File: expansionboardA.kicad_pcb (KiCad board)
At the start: 2 copper layers, 111 x 109.4 mm, 40 parts, among them J1 DEBUG, J2 USB_A_Stacked, J3 HDMI_A, P1 USB_C_Plug, U1 MAX3420EECJ, U2 GPIO_U2, U3 AMS1117-3.3, U4 GPIO_U4, U5 MCP3008T-I/SL, U6 TLV320AIC23BIPW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

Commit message: Updatre board version
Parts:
- removed AU2: SJ-3523-SMT-TR, SJ-3523-SMT-TR:CUI_SJ-3523-SMT-TR
- removed D6: LED, LED_SMD:LED_1206_3216Metric_Pad1.42x1.75mm_HandSolder
- added C10: 0.1uf, Capacitor_SMD:C_0603_1608Metric_Pad1.08x0.95mm_HandSolder, B.Cu at (56.7, 76.6)
- added C11: 3.3uf, Capacitor_THT:CP_Radial_D5.0mm_P2.50mm, F.Cu at (57.7, 72.2)
- added C12: 10uf, Capacitor_THT:CP_Radial_D5.0mm_P2.50mm, F.Cu at (65.6, 76.0)
- added C13: 3.3uf, Capacitor_THT:CP_Radial_D5.0mm_P2.50mm, F.Cu at (98.3, 34.2)
- added C14: 3.3uf, Capacitor_THT:CP_Radial_D5.0mm_P2.50mm, F.Cu at (98.3, 24.6)
- added C8: 1uf ceramic, Capacitor_SMD:C_0603_1608Metric_Pad1.08x0.95mm_HandSolder, F.Cu at (110.5, 28.2)
- added C9: 1uf ceramic, Capacitor_SMD:C_0603_1608Metric_Pad1.08x0.95mm_HandSolder, F.Cu at (110.5, 37.6)
- added R11: 10KOhm, Resistor_SMD:R_0603_1608Metric_Pad0.98x0.95mm_HandSolder, F.Cu at (105.9, 37.6)
- added R12: 470Ohm, Resistor_SMD:R_0603_1608Metric_Pad0.98x0.95mm_HandSolder, F.Cu at (105.9, 34.1)
- added R13: 470Ohm, Resistor_SMD:R_0603_1608Metric_Pad0.98x0.95mm_HandSolder, F.Cu at (105.9, 24.6)
- added R14: 10KOhm, Resistor_SMD:R_0603_1608Metric_Pad0.98x0.95mm_HandSolder, F.Cu at (105.9, 28.2)
- added R8: R33_ohm, Resistor_SMD:R_0603_1608Metric_Pad0.98x0.95mm_HandSolder, F.Cu at (110.5, 34.1)
- AU1: moved to B.Cu
- U6: value TLV320AIC23BIPW -> CS4344-CZZR; footprint TLV320AIC23BIPW:SOP65P640X120-28N -> footprints:CIR_3TSSOP-10; moved to B.Cu
- moved R7 58.8 mm to (110.5, 24.6), turned to 0 degrees
- moved D5 19.2 mm to (74.5, 25.8), turned to 180 degrees
- moved D4 16.6 mm to (74.5, 29.2), turned to 180 degrees
- moved D3 15.1 mm to (74.5, 32.6), turned to 180 degrees
- moved D2 15.0 mm to (74.5, 36.0), turned to 180 degrees
- moved AU1 14.8 mm to (129.0, 29.2)
- moved R6 13.9 mm to (68.7, 25.8), turned to 0 degrees
- moved R5 9.96 mm to (68.7, 29.2), turned to 0 degrees
- moved R4 7.14 mm to (68.7, 32.6), turned to 0 degrees
- moved R3 6.99 mm to (68.7, 36.0), turned to 0 degrees
- moved U6 6.54 mm to (59.8, 81.7), turned to 0 degrees
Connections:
- AU1 pad 2: HPOUTRIGHT -> Net-(AU1-Pad2)
- AU1 pad 3: HPOUTLEFT -> Net-(AU1-Pad3)
- R7 pad 1: LED4 -> LEFTOUT
- R7 pad 2: Net-(D6-A) -> Net-(AU1-Pad3)
- U2 pad 29: I2SCLK -> AU_SDIN
- U2 pad 31: I2SDIN -> AU_SCLK
- U2 pad 33: ASCLK -> AU_LRCLK
- U2 pad 35: ASDIN -> AU_MCLK
- U2 pad 37: AMODE -> unconnected-(U2-Pin_37-Pad37)
- U2 pad 39: ACS -> unconnected-(U2-Pin_39-Pad39)
- U2 pad 53: LED4 -> unconnected-(U2-Pin_53-Pad53)
- U6 pad 1: /input3v3 -> AU_SDIN
- U6 pad 10: HPOUTRIGHT -> /AR
- U6 pad 2: unconnected-(U6-CLKOUT-Pad2) -> AU_SCLK
- U6 pad 3: I2SCLK -> AU_LRCLK
- U6 pad 4: I2SDIN -> AU_MCLK
- U6 pad 5: unconnected-(U6-LRCIN-Pad5) -> Net-(U6-VQ)
- U6 pad 6: unconnected-(U6-DOUT-Pad6) -> Net-(U6-FILT+)
- U6 pad 7: unconnected-(U6-LRCOUT-Pad7) -> /AL
- U6 pad 8: /input3v3 -> GND
- U6 pad 9: HPOUTLEFT -> unconnected-(U6-VA-Pad9)
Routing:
- net HPOUTLEFT: track 91.9 -> 0.00 mm, vias 2 -> 0
- net LINEOUTLEFT: track 91.7 -> 0.00 mm, vias 2 -> 0
- net LINEOUTRIGHT: track 91.6 -> 0.00 mm, vias 2 -> 0
- net HPOUTRIGHT: track 91.4 -> 0.00 mm, vias 2 -> 0
- net /AL: track 0.00 -> 83.0 mm, vias 0 -> 1
- net /AR: track 0.00 -> 78.3 mm, vias 0 -> 1
- net LED4: track 29.6 -> 0.00 mm
- net Net-(AU1-Pad3): track 0.00 -> 20.7 mm, vias 0 -> 1
- net I2SCLK: track 18.1 -> 0.00 mm, vias 1 -> 0
- net I2SDIN: track 17.4 -> 0.00 mm, vias 1 -> 0
- net /input3v3: track 191.2 -> 174.6 mm, vias 8 -> 6
- net Net-(AU1-Pad2): track 0.00 -> 13.3 mm, vias 0 -> 1
- net ASCLK: track 11.3 -> 0.00 mm
- net AU_LRCLK: track 0.00 -> 11.0 mm
- net AU_SDIN: track 0.00 -> 11.0 mm
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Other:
- board text added: "GND D+ D- 5V"
- board text removed: "5V D- D+ GND"
- board text removed: "LINE OUT"

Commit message: Updated board files
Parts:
- moved D5 24.3 mm to (50.4, 22.7), turned to -90 degrees
- moved D4 21.7 mm to (53.8, 22.7), turned to -90 degrees
- moved D3 19.9 mm to (57.2, 22.7), turned to -90 degrees
- moved D2 19.3 mm to (60.6, 22.7), turned to -90 degrees
- moved R6 18.5 mm to (50.4, 28.5), turned to 90 degrees
- moved R5 14.9 mm to (53.8, 28.5), turned to 90 degrees
- moved R4 12.2 mm to (57.2, 28.5), turned to 90 degrees
- moved R3 11.0 mm to (60.6, 28.5), turned to 90 degrees
- moved C3 1.80 mm to (89.2, 86.9)
- moved C4 1.80 mm to (81.9, 94.1)
- moved Y1 1.80 mm to (84.6, 91.5)
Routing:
- net LED3: track 41.6 -> 44.7 mm
- net USBD1_N: track 31.9 -> 34.9 mm
- net USBD1_P: track 31.8 -> 34.7 mm
- net Net-(U1-XO): track 10.9 -> 8.90 mm
- net LED2: track 40.2 -> 42.1 mm
- net Net-(U1-XI): track 11.3 -> 9.47 mm
- net LED0: track 41.0 -> 42.3 mm
- net LED1: track 39.8 -> 40.9 mm
- net Net-(U6-VQ): track 10.0 -> 10.7 mm
- net GND: vias 28 -> 27

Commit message: Updated board to fix some issues
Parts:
- added J4: FAN, Connector_PinHeader_2.54mm:PinHeader_1x02_P2.54mm_Vertical, F.Cu at (38.3, 114.2)
- J1: footprint Connector_PinSocket_2.54mm:PinSocket_1x04_P2.54mm_Vertical -> Connector_PinSocket_2.54mm:PinSocket_1x04_P2.54mm_Horizontal; moved to B.Cu
- moved J1 8.07 mm to (122.6, 110.7), turned to 180 degrees
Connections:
- U6 pad 9: unconnected-(U6-VA-Pad9) -> /input3v3
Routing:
- net /input3v3: track 174.6 -> 207.4 mm
- net TXD: track 7.60 -> 14.0 mm
- net RXD: track 7.60 -> 14.0 mm
- net 5V: track 316.6 -> 318.9 mm
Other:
- board text added: "+"
- board text added: "AD/C"
- board text added: "Copyright 2023 Engin Cilasun issue 1C"
- board text added: "FAN"
- board text added: "HEADPHONES"
- board text added: "INT3v3"
- board text added: "REG3v3"
- board text removed: "ADC"
- board text removed: "Copyright 2023 Engin Cilasun issue 1B"
- board text removed: "HEADPHONE"
- board text removed: "INT"
- board text removed: "REG"

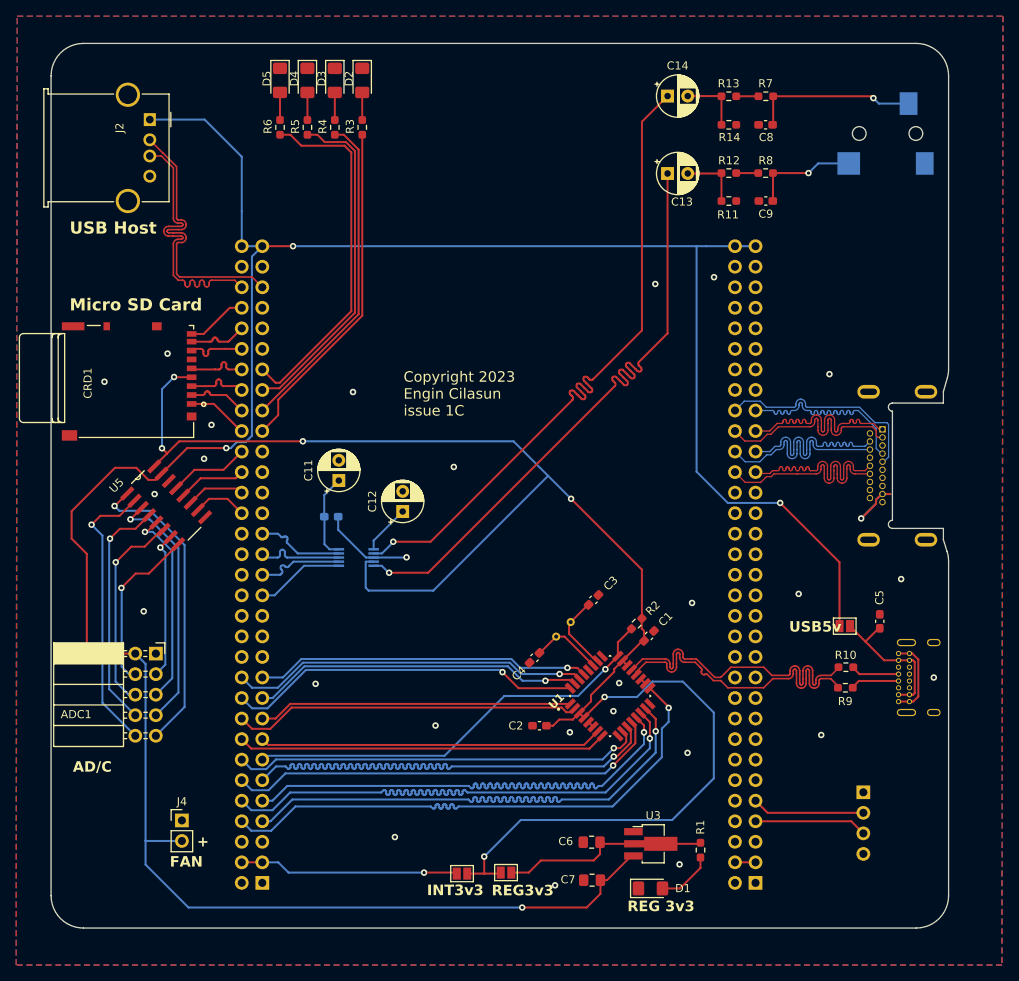
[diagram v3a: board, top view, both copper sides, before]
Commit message: Updated to new board version
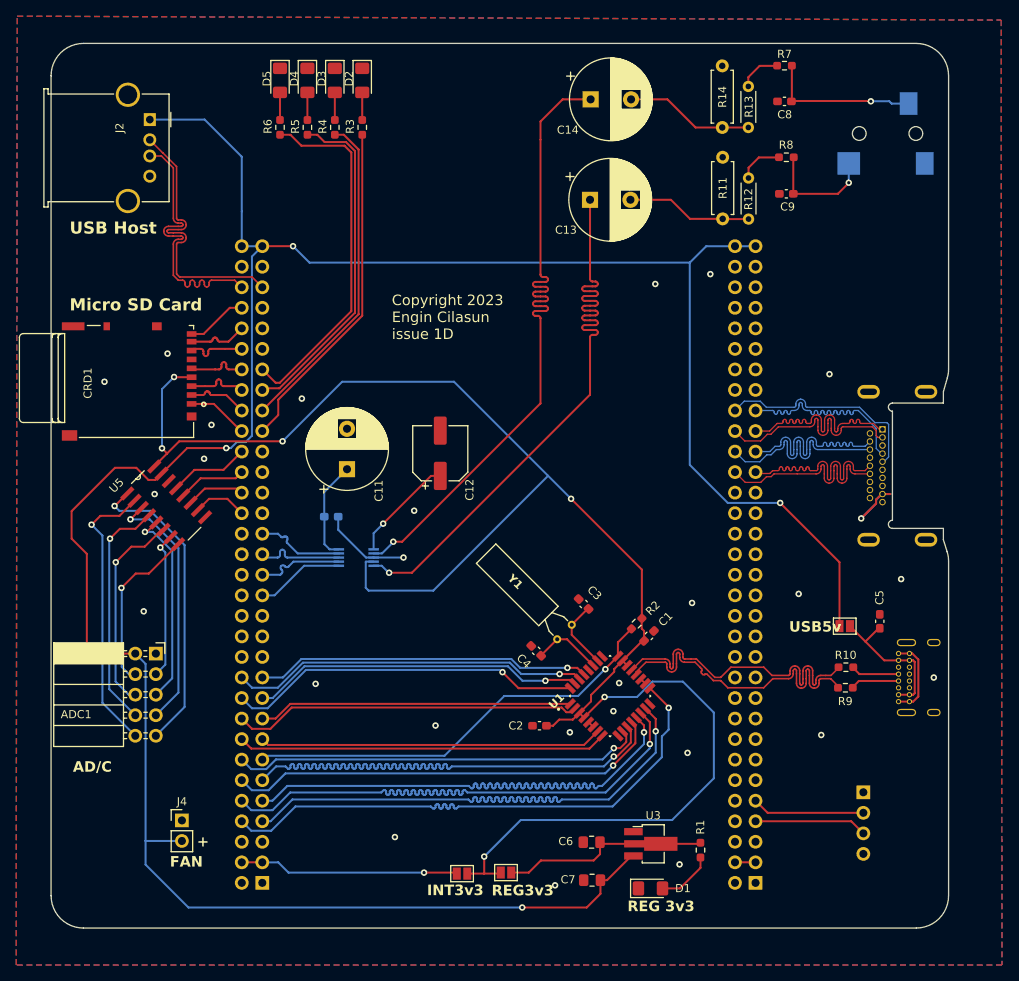
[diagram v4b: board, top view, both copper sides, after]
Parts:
- C11, C13, C14: footprint Capacitor_THT:CP_Radial_D5.0mm_P2.50mm -> Capacitor_THT:CP_Radial_D10.0mm_P5.00mm
- C12: footprint Capacitor_THT:CP_Radial_D5.0mm_P2.50mm -> Capacitor_SMD:CP_Elec_6.3x5.9
- R11, R14: footprint Resistor_SMD:R_0603_1608Metric_Pad0.98x0.95mm_HandSolder -> Resistor_THT:R_Axial_DIN0207_L6.3mm_D2.5mm_P7.62mm_Horizontal
- R12, R13: footprint Resistor_SMD:R_0603_1608Metric_Pad0.98x0.95mm_HandSolder -> Resistor_THT:R_Axial_DIN0204_L3.6mm_D1.6mm_P5.08mm_Horizontal
- Y1: moved to F.Cu
- moved C13 10.1 mm to (88.8, 37.4)
- moved C14 9.52 mm to (88.8, 25.0)
- moved C12 8.58 mm to (70.2, 68.8)
- moved R12 6.19 mm to (108.4, 39.8), turned to 90 degrees
- moved R13 4.55 mm to (108.3, 28.5), turned to 90 degrees
- moved R7 4.43 mm to (112.8, 20.9)
- moved C8 3.72 mm to (112.8, 25.3)
- moved R8 3.23 mm to (113.0, 32.2)
- moved C9 2.69 mm to (113.0, 36.7)
- moved Y1 2.42 mm to (86.5, 90.0), turned to -135 degrees
- moved R11 2.34 mm to (105.2, 39.8), turned to 90 degrees
- moved C11 1.73 mm to (58.7, 70.8)
- moved C3 1.32 mm to (88.0, 87.4), turned to -45 degrees
- moved C4 0.89 mm to (82.1, 93.2), turned to -45 degrees
- moved R14 0.88 mm to (105.1, 28.5), turned to 90 degrees
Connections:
- Y1 pad 1: Net-(U1-XO) -> Net-(U1-XI)
- Y1 pad 2: Net-(U1-XI) -> Net-(U1-XO)
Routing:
- net Net-(C14-Pad2): track 7.71 -> 15.9 mm
- net Net-(C13-Pad2): track 7.64 -> 15.6 mm
- net Net-(U6-FILT+): track 6.16 -> 13.2 mm, vias 0 -> 1
- net /input3v3: track 207.4 -> 213.5 mm
- net RIGHTOUT: track 2.72 -> 5.57 mm
- net LEFTOUT: track 2.75 -> 5.29 mm
- net Net-(U6-VQ): track 10.7 -> 12.5 mm
- net Net-(AU1-Pad3): track 20.7 -> 18.9 mm
- net Net-(AU1-Pad2): track 13.3 -> 14.4 mm
- net Net-(U1-XI): track 9.47 -> 8.68 mm
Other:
- board text added: "Copyright 2023 Engin Cilasun issue 1D"
- board text added: "USB-C POWER"
- board text added: "VIDEO OUT"
- board text removed: "Copyright 2023 Engin Cilasun issue 1C"
- board text removed: "DVI OUT"
- board text removed: "USB-C Power"
